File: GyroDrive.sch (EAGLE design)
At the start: 35 parts, among them Q1 TF412ST5G, Q2 TF412ST5G, Q3 TF412ST5G, Q4 TF412ST5G, Q5 TF412ST5G, Q6 TF412ST5G

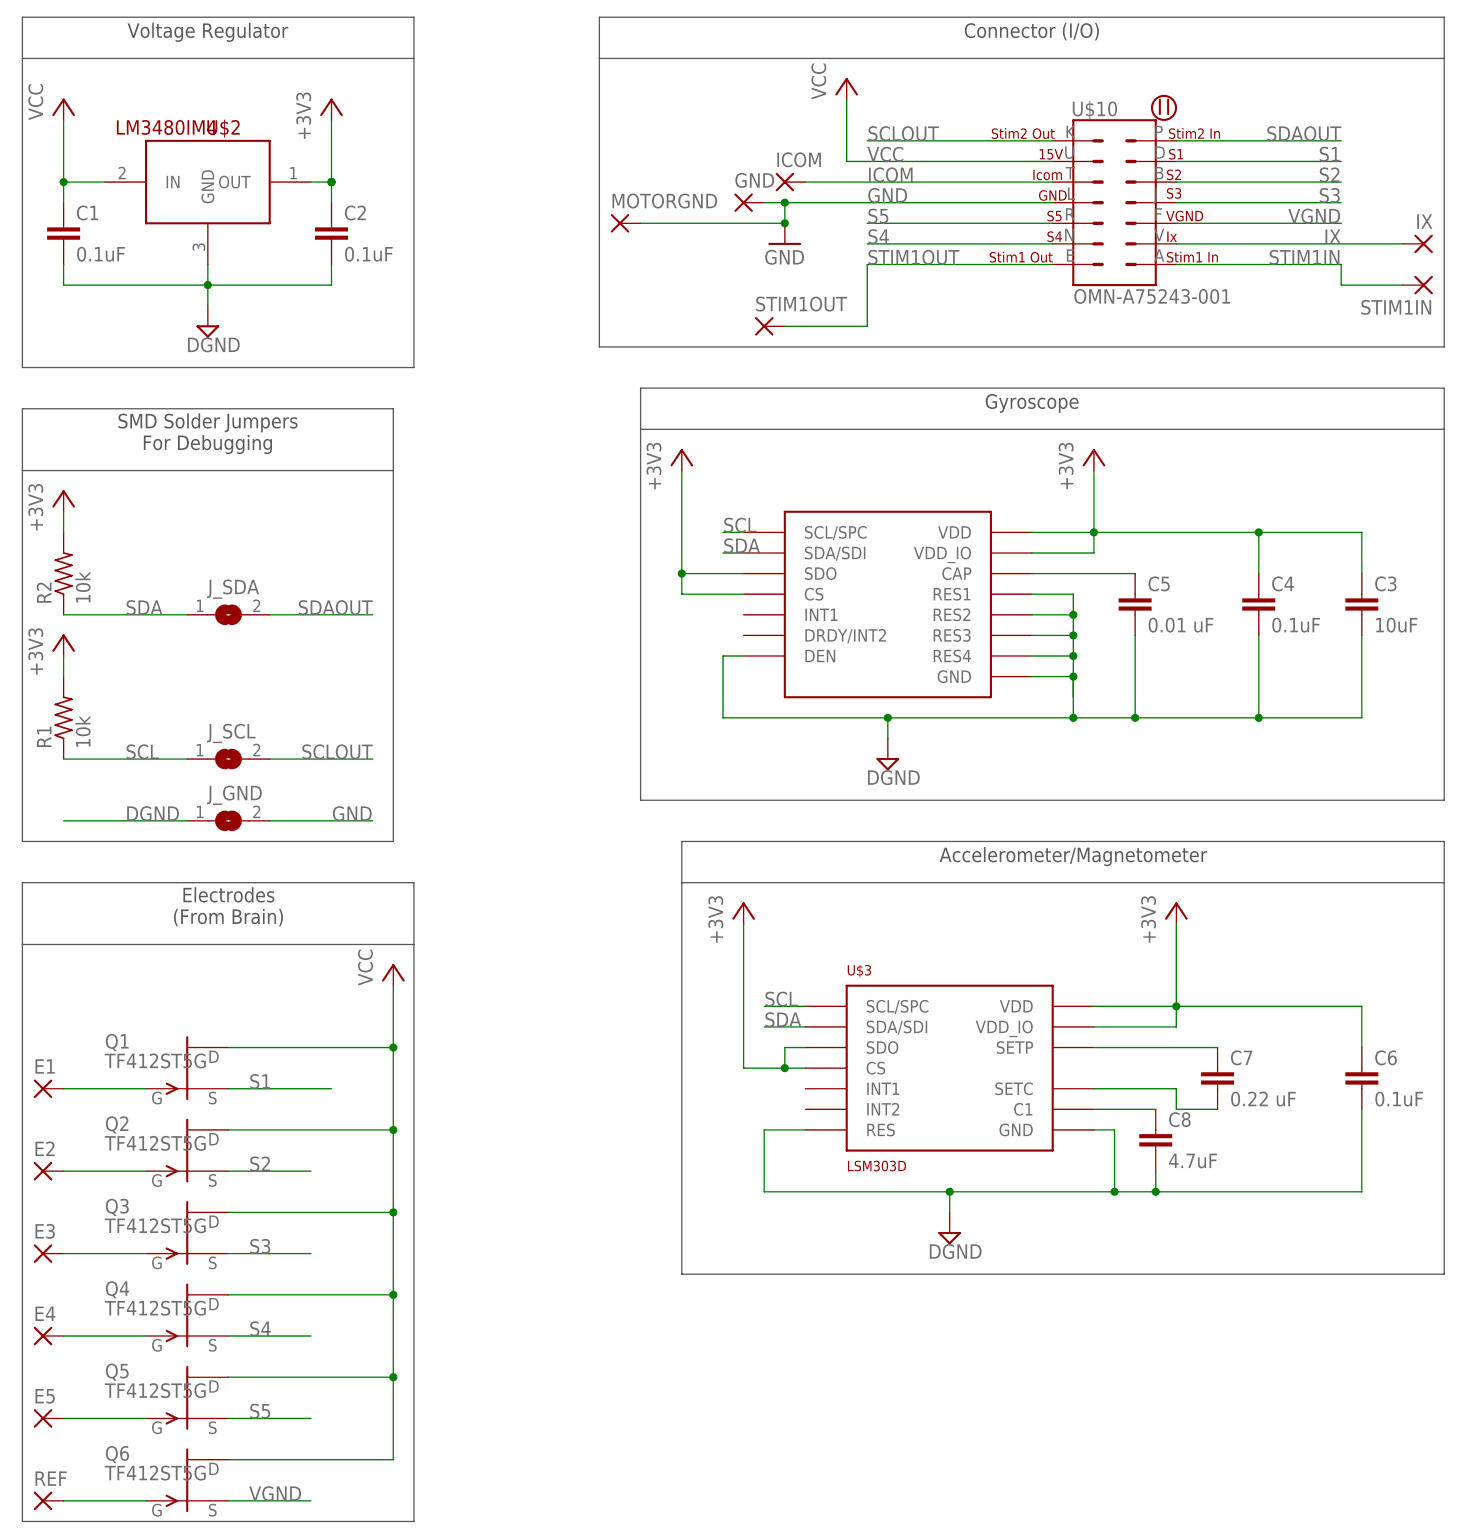
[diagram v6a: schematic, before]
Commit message: Switched to Invensense MPU-9250
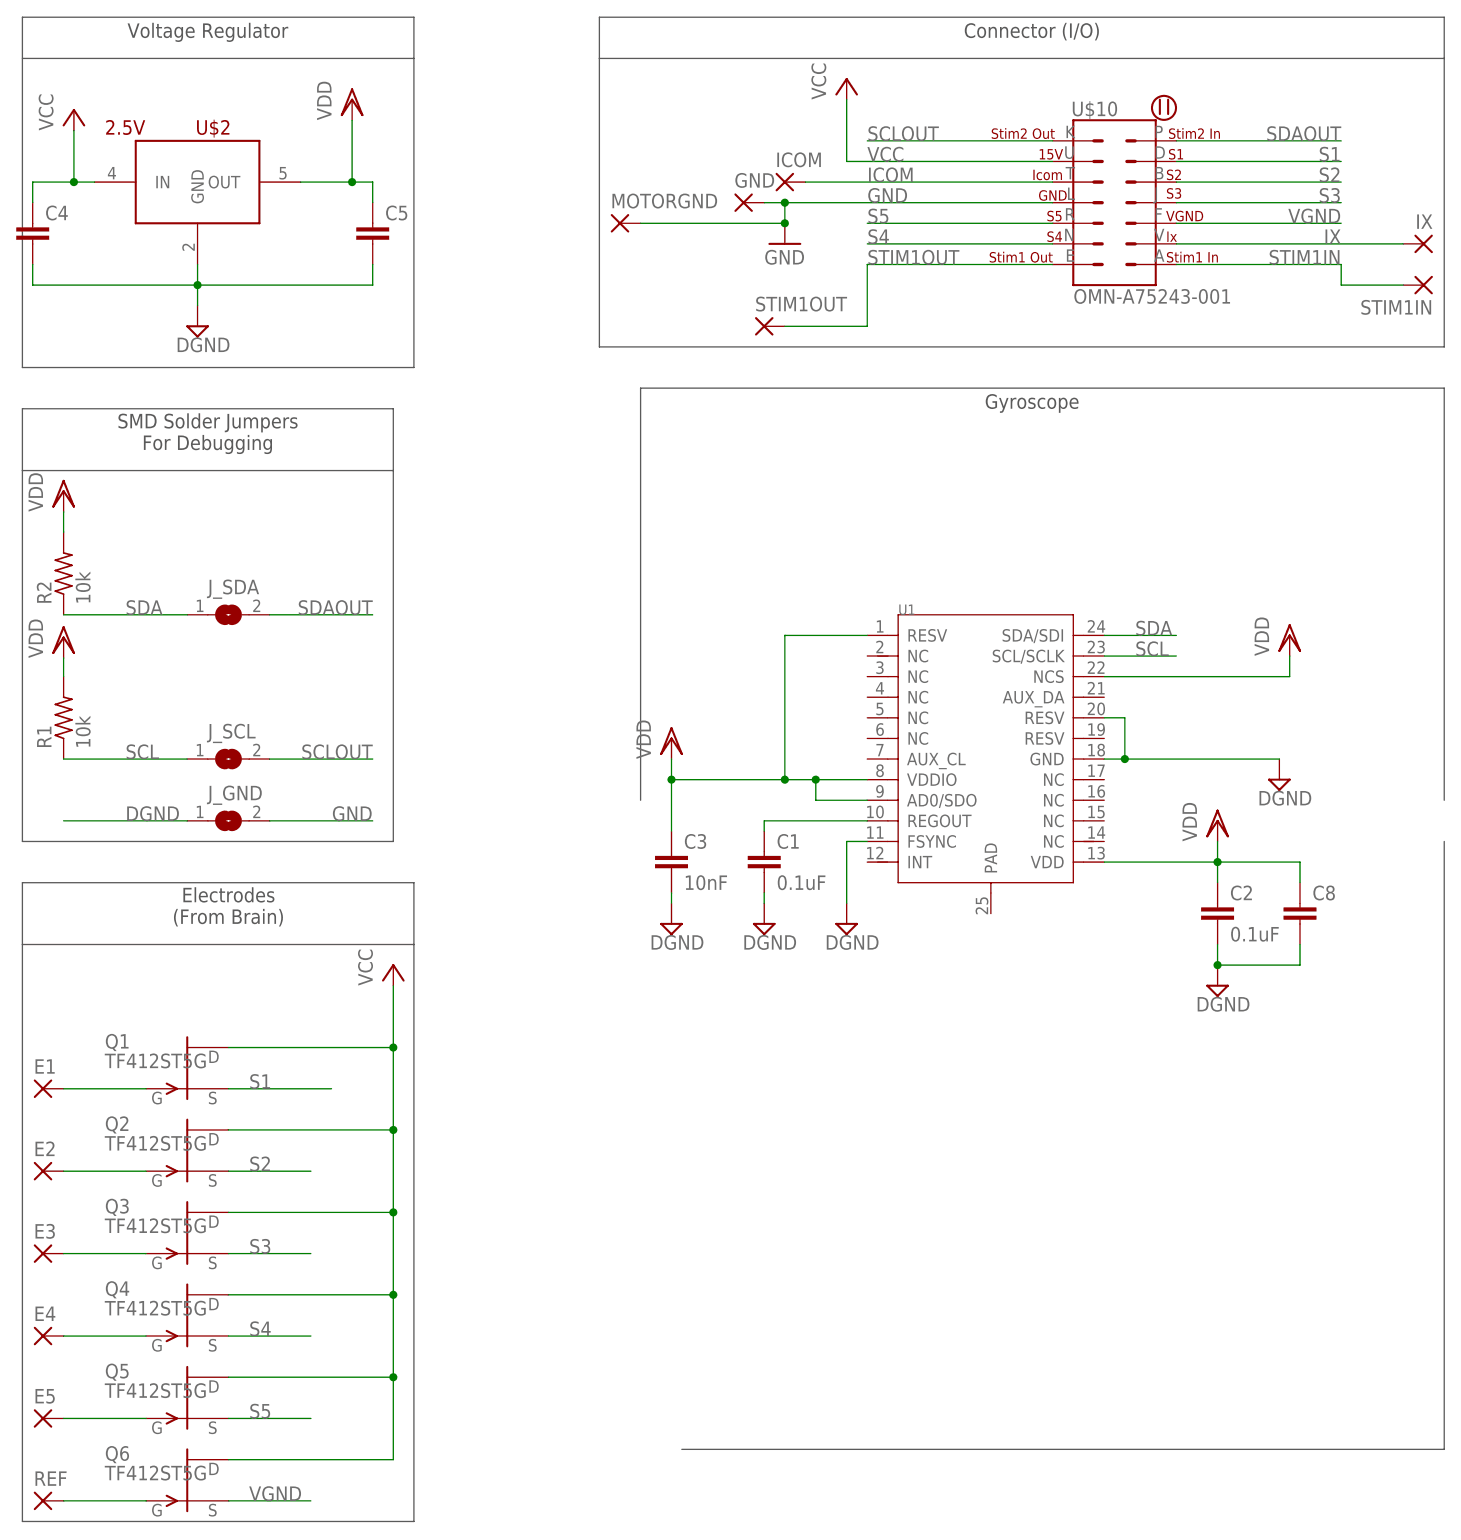
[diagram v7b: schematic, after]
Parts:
- removed C6: 0.1uF, resistor:C-EUC0201
- removed C7: 0.22 uF, resistor:C-EUC0201
- removed U$1: L3GD20H, st:L3GD20H
- removed U$3: LSM303D, st:LSM303D
- added U1: (no value), Grove - IMU 10DOF v1.1:MPU-9250
- C1, C2: device resistor:C-EUC0201 -> resistor:C-EUC0402
- C3: value 10uF -> 10nF; device resistor:C-EUC0603 -> resistor:C-EUC0402
- C4: value 0.1uF -> (none); device resistor:C-EUC0201 -> resistor:C-EUC0402
- C5: value 0.01 uF -> (none)
- C8: value 4.7uF -> (none); device resistor:C-EUC0402 -> resistor:C-EUC0603
- U$2: value LM3480IM4 -> 2.5V; device SparkFun-PowerIC:LM3480IM4 -> michael-stetner:TPS715-FIXED
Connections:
- removed net +3V3: C2.1, C3.1, C4.1, C6.1, R1.2, R2.2, U$1.CS, U$1.SDO, U$1.VDD, U$1.VDD_IO, U$2.OUT, U$3.CS, U$3.SDO, U$3.VDD, U$3.VDD_IO
- removed net N$1: C8.1, U$3.C1
- removed net N$3: C7.2, U$3.SETC
- removed net N$9: C5.1, U$1.CAP
- new net VDD: C2.1, C3.1, C5.1, C8.1, R1.2, R2.2, U$2.OUT, U1.AD0/SDO, U1.NCS, U1.RESV, U1.VDD, U1.VDDIO
- net DGND: now also U1.FSYNC, U1.GND, U1.RESV@2; no longer C6.2, U$1.DEN, U$1.GND, U$1.RES1, U$1.RES2, U$1.RES3, U$1.RES4, U$3.GND, U$3.RES
- net N$2: now also C1.1, U1.REGOUT; no longer C7.1, U$3.SETP
- net SCL: now also U1.SCL/SCLK; no longer U$1.SCL/SPC, U$3.SCL/SPC
- net SDA: now also U1.SDA/SDI; no longer U$1.SDA/SDI, U$3.SDA/SDI
- net VCC: now also C4.1; no longer C1.1
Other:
- note removed: "Accelerometer/Magnetometer"
- moved on the sheet: C1, C2, C3, C4, C5, C8, U$2
